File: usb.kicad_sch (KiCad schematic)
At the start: 12 parts, among them J10 USB_C_Receptacle_USB2.0, Q4 MMBT5401, Q5 AO3401A, Q6 MMBT5401

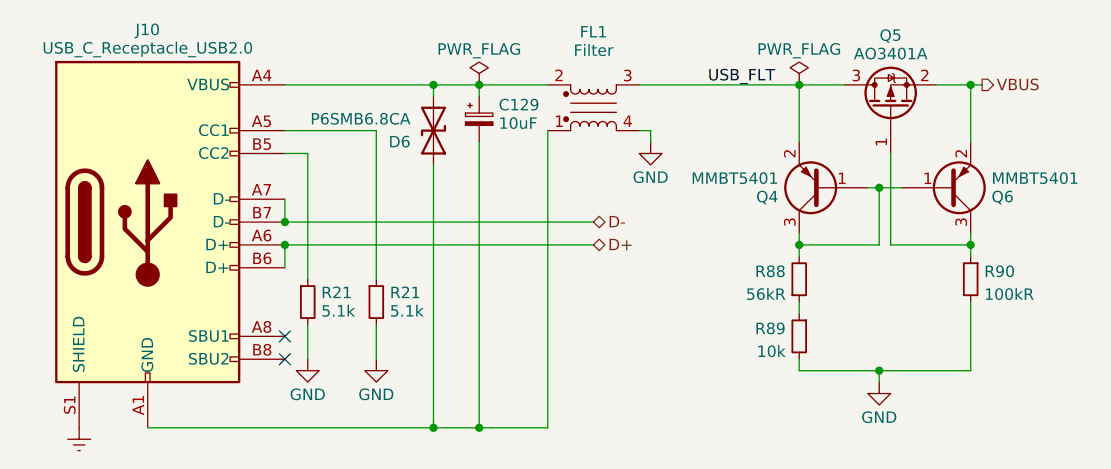
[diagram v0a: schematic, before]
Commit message: Connect shield net to second USB port
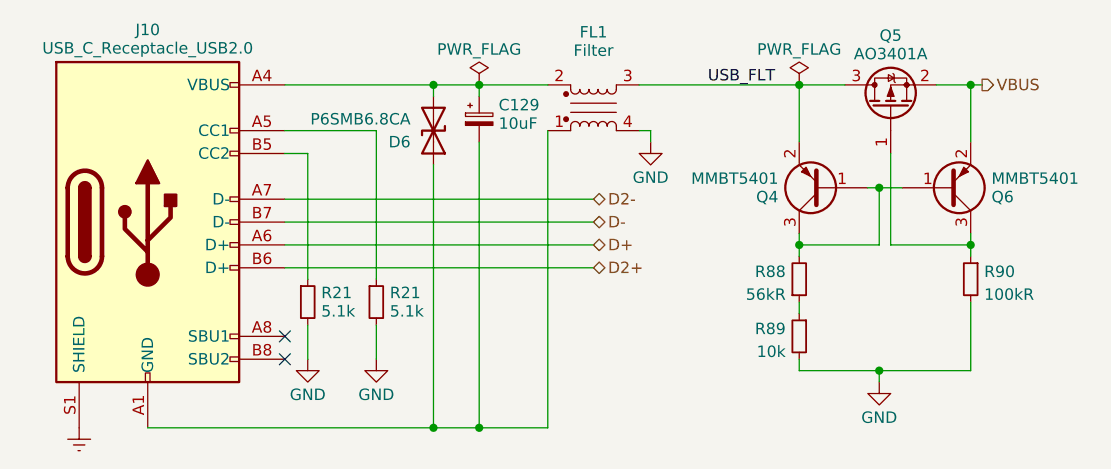
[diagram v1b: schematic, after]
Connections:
- net D+: no longer J10.B6 (D+)
- net D-: no longer J10.A7 (D-)
- new net D2+: J10.B6 (D+)
- new net D2-: J10.A7 (D-)
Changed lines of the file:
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@@
   (junction (at 154.94 78.74) (diameter 0) (color 0 0 0 0)
-  )
-  (junction (at 78.74 78.74) (diameter 0) (color 0 0 0 0)
   )
   (junction (at 144.78 72.39) (diameter 0) (color 0 0 0 0)
@@
   )
   (junction (at 135.89 78.74) (diameter 0) (color 0 0 0 0)
-  )
-  (junction (at 78.74 76.2) (diameter 0) (color 0 0 0 0)
   )
   (junction (at 135.89 60.96) (diameter 0) (color 0 0 0 0)
@@
   )
   (wire (pts (xy 154.94 77.47) (xy 154.94 78.74))
-    (stroke (width 0) (type default))
-  )
-  (wire (pts (xy 78.74 78.74) (xy 78.74 81.28))
     (stroke (width 0) (type default))
   )
@@
   )
   (wire (pts (xy 78.74 78.74) (xy 113.03 78.74))
+    (stroke (width 0) (type default))
+  )
+  (wire (pts (xy 78.74 73.66) (xy 113.03 73.66))
     (stroke (width 0) (type default))
   )
@@
     (stroke (width 0) (type default))
   )
+  (wire (pts (xy 78.74 81.28) (xy 113.03 81.28))
+    (stroke (width 0) (type default))
+  )
   (wire (pts (xy 144.78 93.98) (xy 144.78 92.71))
     (stroke (width 0) (type default))
@@
   )
   (wire (pts (xy 100.33 67.31) (xy 100.33 99.06))
-    (stroke (width 0) (type default))
-  )
-  (wire (pts (xy 78.74 73.66) (xy 78.74 76.2))
     (stroke (width 0) (type default))
   )
@@
     (effects (font (size 1.27 1.27)) (justify left))
   )
+  (hierarchical_label "D2-" (shape bidirectional) (at 113.03 73.66 0) (fields_autoplaced)
+    (effects (font (size 1.27 1.27)) (justify left))
+  )
+  (hierarchical_label "D2+" (shape bidirectional) (at 113.03 81.28 0) (fields_autoplaced)
+    (effects (font (size 1.27 1.27)) (justify left))
+  )

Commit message: Fix LCSC part numbers
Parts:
- J10: LCSC (none) -> C167321
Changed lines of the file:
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@@
+      (effects (font (size 1.27 1.27)) hide)
+    )
+    (property "LCSC" "C167321" (at 63.5 76.2 0)
       (effects (font (size 1.27 1.27)) hide)
     )
